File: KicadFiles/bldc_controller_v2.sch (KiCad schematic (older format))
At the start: 183 parts, among them J1 Conn_01x06_Male, J10 Conn_01x02_Female, J11 Conn_01x02_Female, J12 Conn_01x02_Female, J13 Conn_01x02_Female, J14 Conn_01x02_Female, J15 Conn_01x04_Male, J2 Conn_01x03_Male, J3 Conn_01x03_Male, J4 Screw_Terminal, J5 Conn_01x02_Female, J9 Conn_01x02_Female, Q1 DMN65D8L-7, Q10 IRLB8721PBF, Q11 IRLB8721PBF, Q2 DMN65D8L-7, Q3 DMN65D8L-7, Q5 IRF4905, Q6 IRLB8721PBF, Q7 IRLB8721PBF, Q8 IRLB8721PBF, Q9 IRLB8721PBF, SW1 D6C50 F1 LFS, SW2 D6C40 F1 LFS, SW3 1301.9314, SW4 1301.9314, SW5 SW_Push_DPDT, U1 ATmega328P-PU, U2 uA7810, U3 LM7805_TO220, U4 MCP601-xP, U5 LM339, U6 IRS2004, U7 IRS2004, U8 IRS2004, U9 NSL-32, Y1 9B-16.000MBBK-B

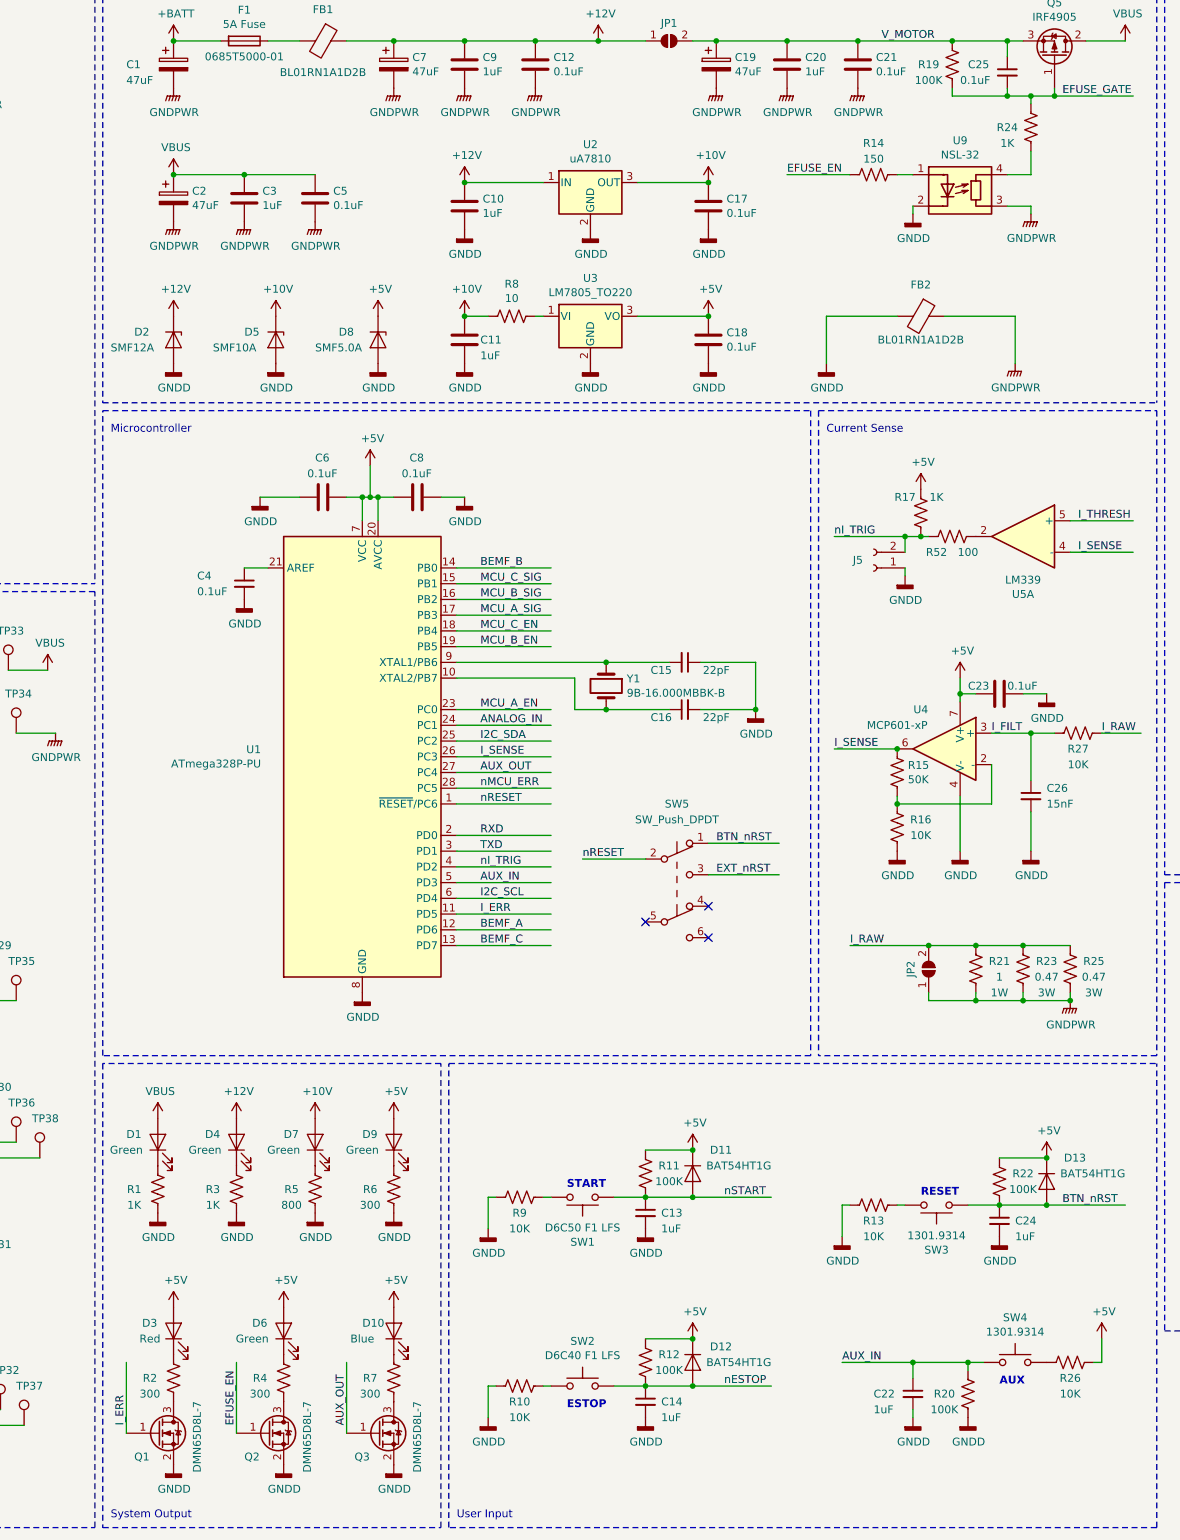
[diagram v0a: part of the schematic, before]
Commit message: Added Optoisolator
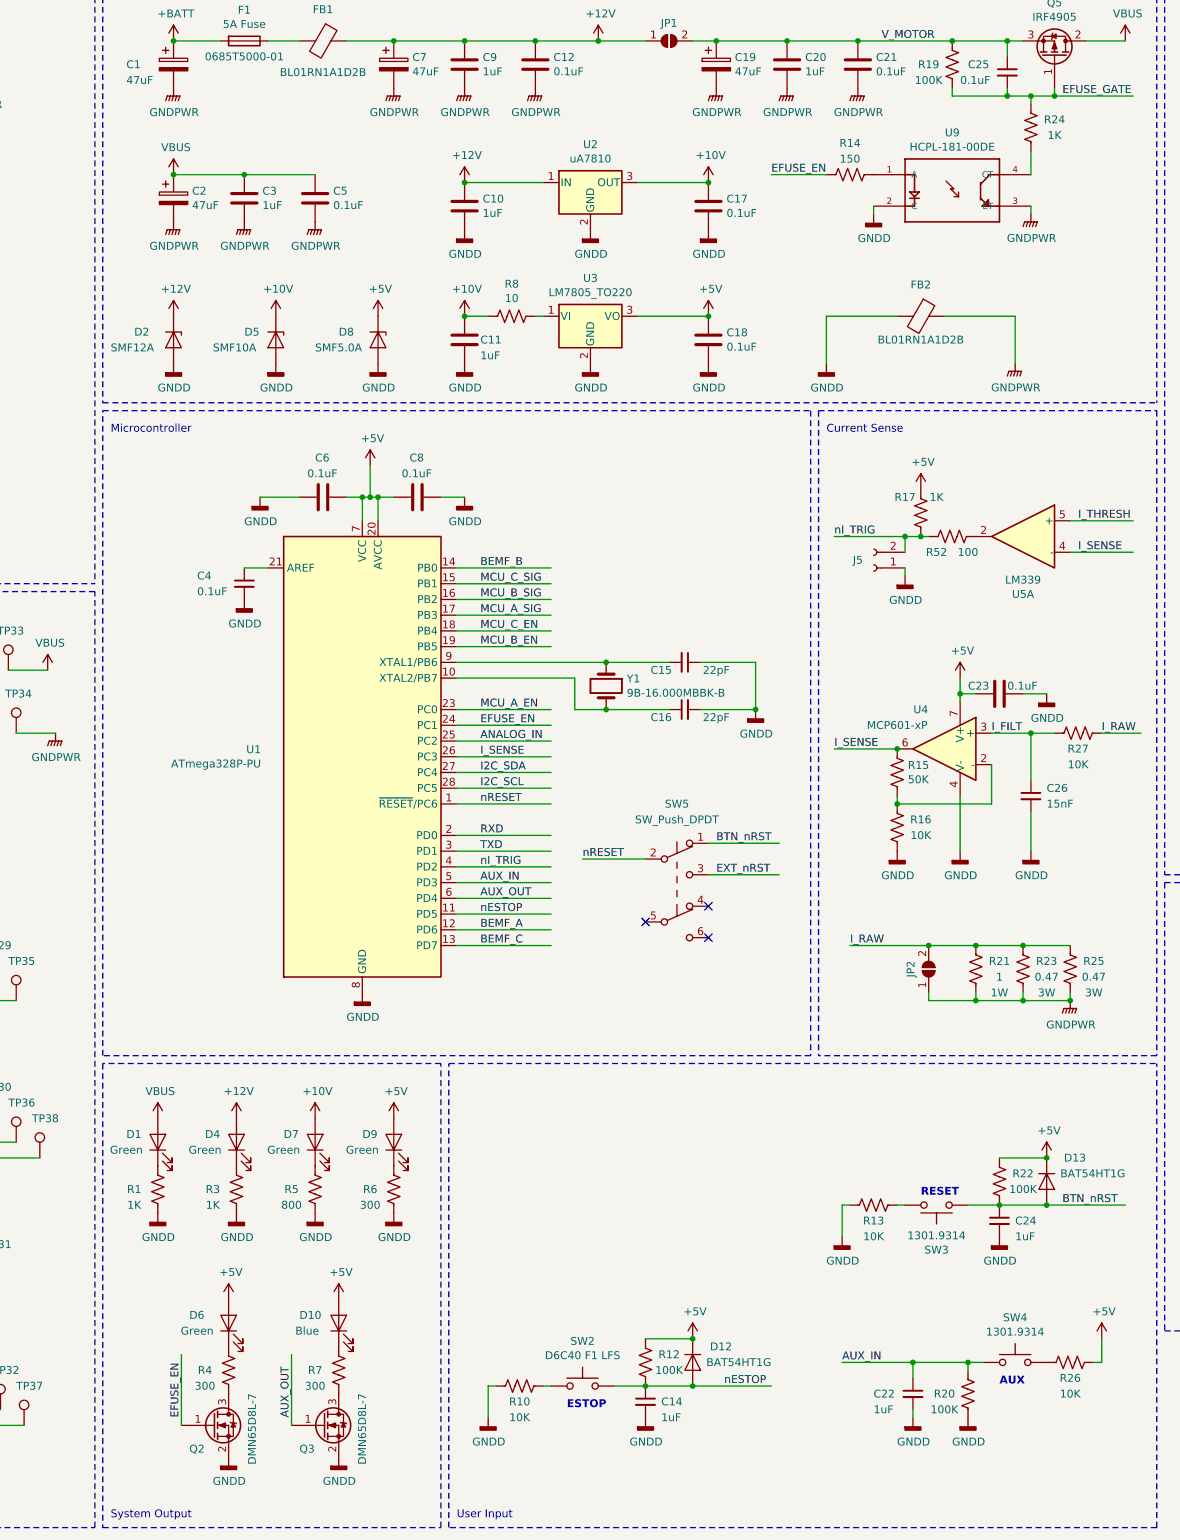
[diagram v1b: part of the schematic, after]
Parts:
- removed C13: 1uF, Capacitor_SMD:C_0805_2012Metric_Pad1.15x1.40mm_HandSolder, symbol Device:C_Small
- removed D11: BAT54HT1G, Diode_SMD:D_SOD-323_HandSoldering, symbol Diode:1N914
- removed D3: LTST-C171KRKT, LED_SMD:LED_0805_2012Metric_Pad1.15x1.40mm_HandSolder, symbol Device:LED
- removed Q1: DMN65D8L-7, Package_TO_SOT_SMD:SOT-23, symbol Transistor_FET:DMN67D7L
- removed R11: 100K, Resistor_SMD:R_0805_2012Metric_Pad1.15x1.40mm_HandSolder, symbol Device:R_US
- removed R2: 300, Resistor_SMD:R_0805_2012Metric_Pad1.15x1.40mm_HandSolder, symbol Device:R_US
- removed R9: 10K, Resistor_SMD:R_0805_2012Metric_Pad1.15x1.40mm_HandSolder, symbol Device:R_US
- removed SW1: D6C50 F1 LFS, Button_Switch_THT:Pushbutton_Switch_TH, symbol Switch:SW_Push
- removed U9: NSL-32, symbol Isolator:NSL-32
- added U9: HCPL-181-00DE, HCPL-181:SOIC254P700X220-4N, symbol HCPL-181-00DE:HCPL-181-00DE
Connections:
- net labels removed: I_ERR, nMCU_ERR, nSTART
- wire segments 340 -> 329
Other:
- note removed: "START"
- moved on the sheet: D10, D6, Q2, Q3, R14, R4, R7

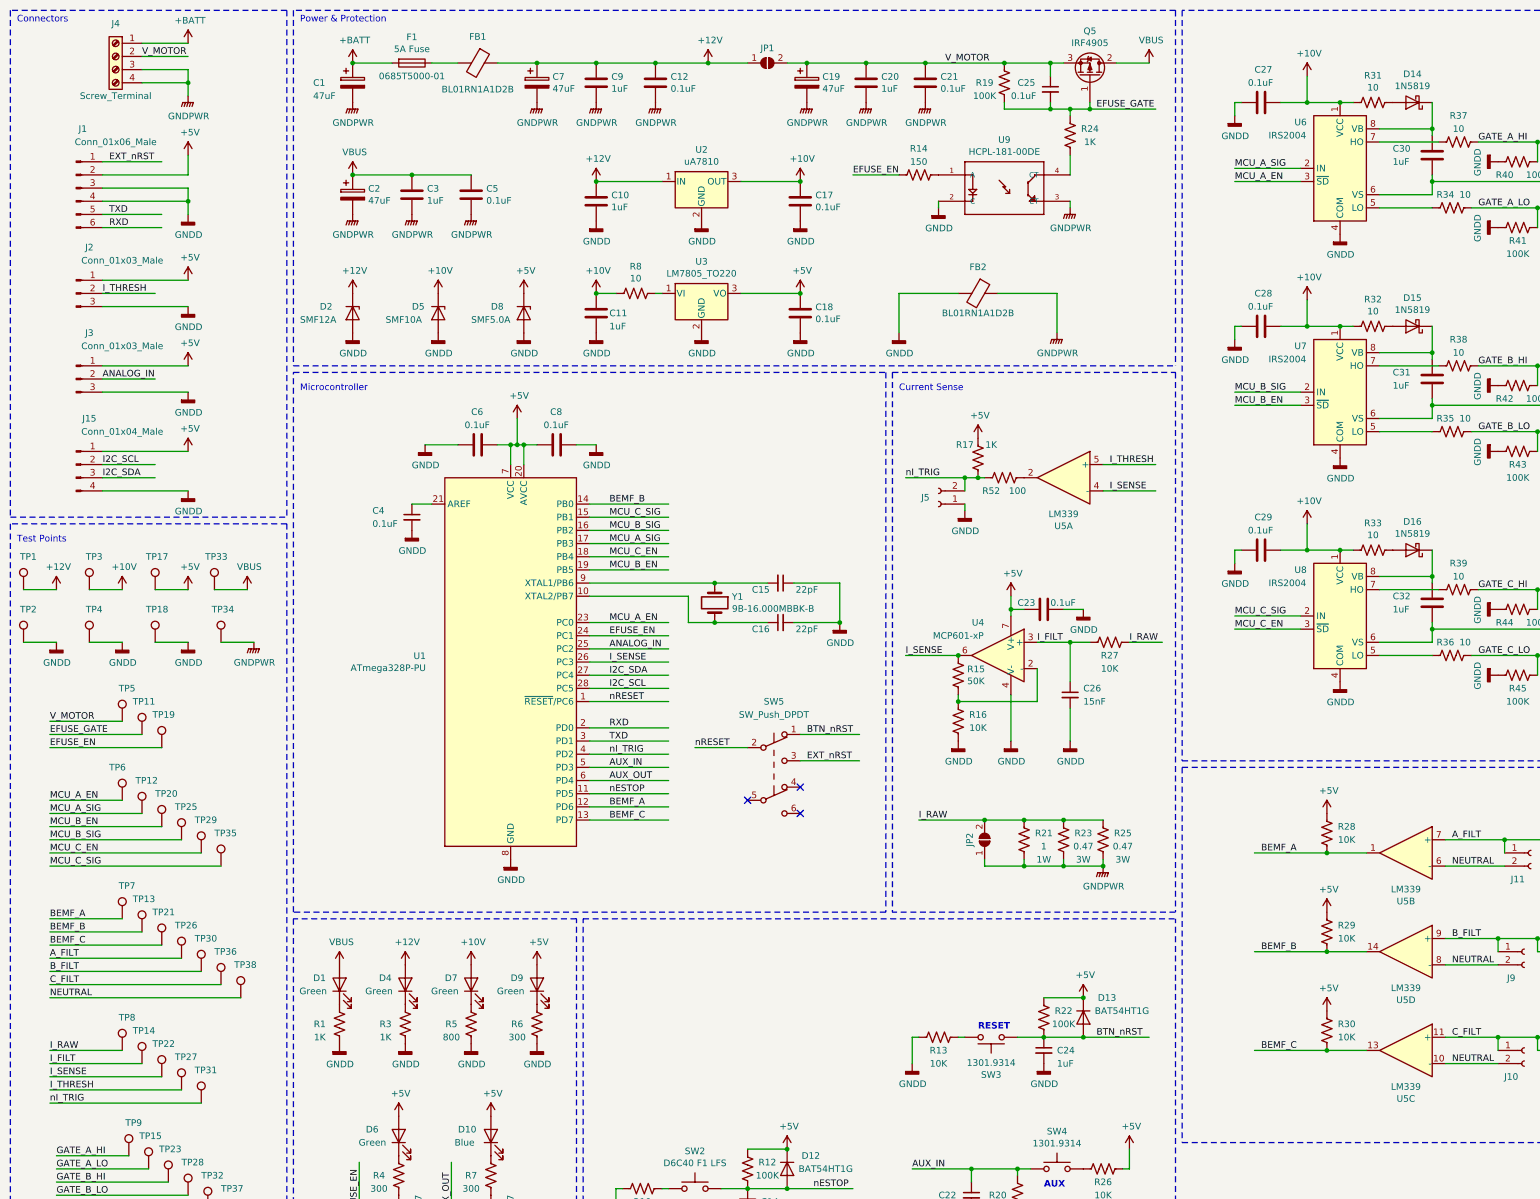
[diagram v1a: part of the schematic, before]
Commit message: Updated Major Parts Placement
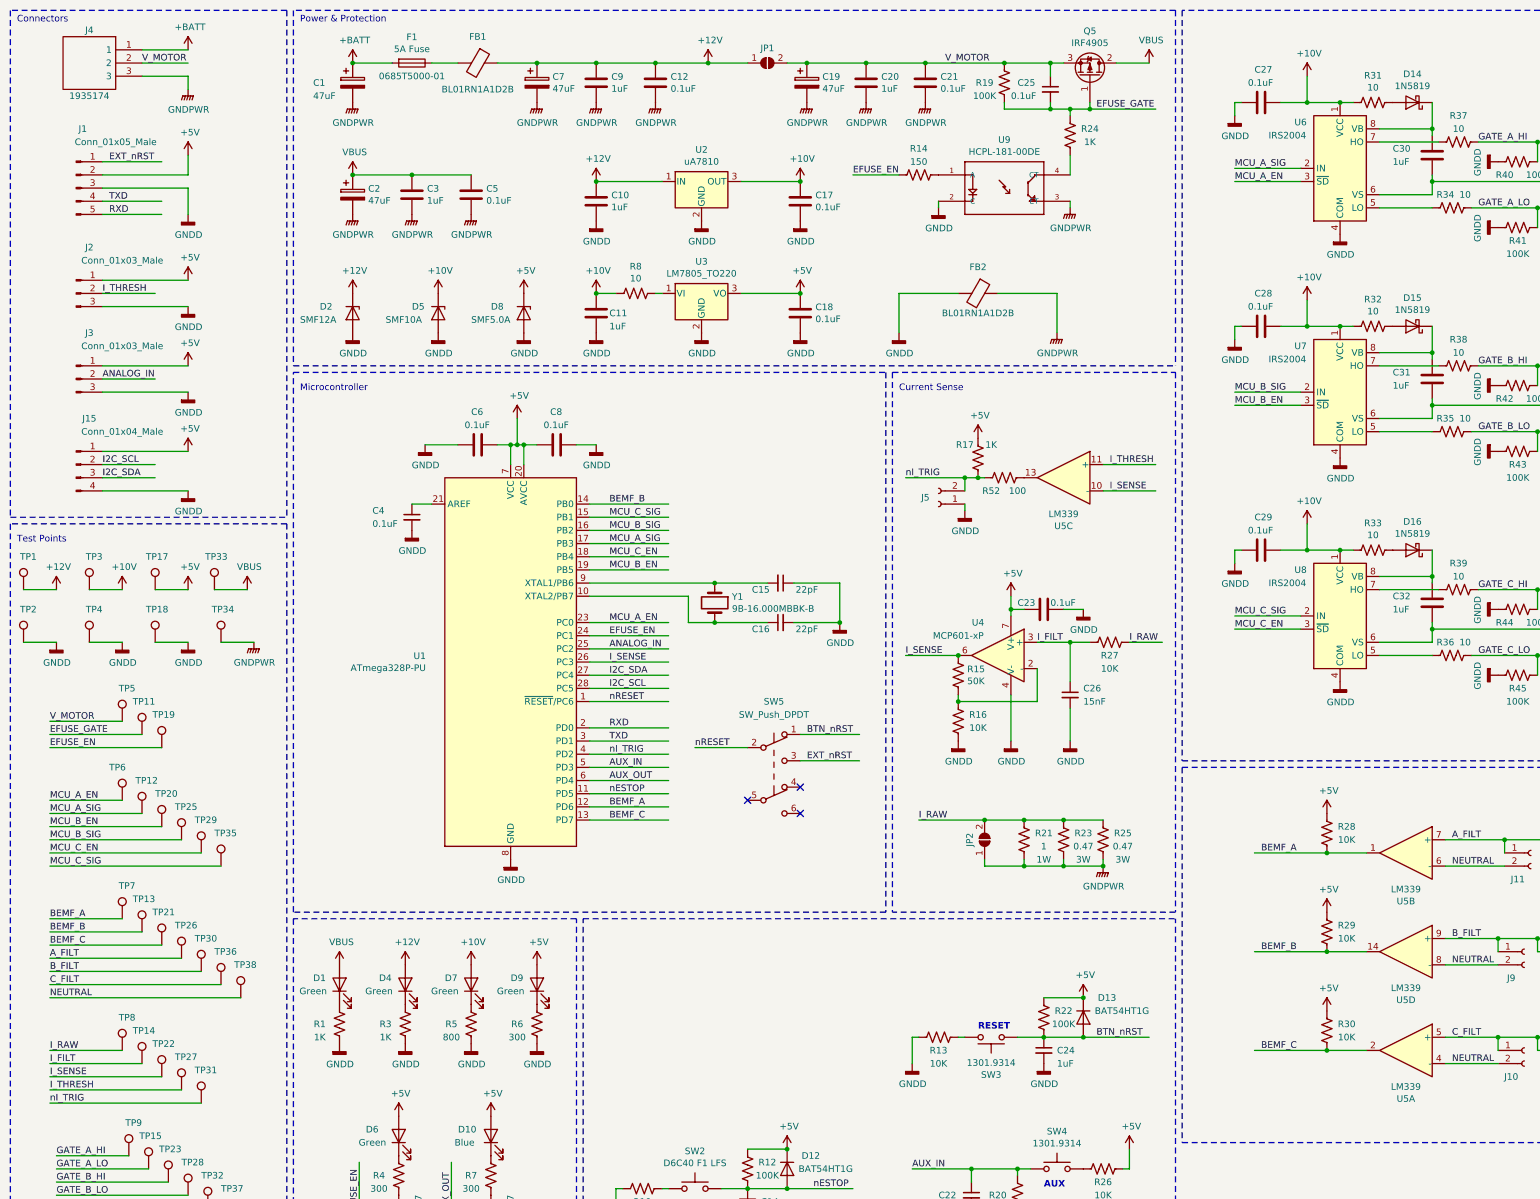
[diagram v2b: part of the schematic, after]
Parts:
- removed J1: Conn_01x06_Male, Connector_PinHeader_2.54mm:PinHeader_1x06_P2.54mm_Vertical, symbol Connector:Conn_01x06_Male
- removed J4: Screw_Terminal, Connector:Terminal_Block_4Pin_TH, symbol Connector:Screw_Terminal_01x04
- added J1: Conn_01x05_Male, Connector_PinHeader_2.54mm:PinHeader_1x05_P2.54mm_Vertical, symbol Connector:Conn_01x05_Male
- added J4: 1935174, 1935174:SHDR3W110P0X500_1X3_1500X900X1140P, symbol 1935174:1935174
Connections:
- wire segments 329 -> 325
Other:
- moved on the sheet: U5A, U5C
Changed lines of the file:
@@
 Text Label 1800 1750 0    50   ~ 0
 EXT_nRST
-Text Label 1800 2150 0    50   ~ 0
+Text Label 1800 2050 0    50   ~ 0
 TXD
-Text Label 1800 2250 0    50   ~ 0
+Text Label 1800 2150 0    50   ~ 0
 RXD
 $Comp
@@
 L power:+BATT #PWR05
 U 1 1 5DC4550F
-P 2400 850
-F 0 "#PWR05" H 2400 700 50  0001 C CNN
-F 1 "+BATT" H 2415 1023 50  0000 C CNN
-F 2 "" H 2400 850 50  0001 C CNN
-F 3 "" H 2400 850 50  0001 C CNN
-	1    2400 850
+P 2400 900
+F 0 "#PWR05" H 2400 750 50  0001 C CNN
+F 1 "+BATT" H 2415 1073 50  0000 C CNN
+F 2 "" H 2400 900 50  0001 C CNN
+F 3 "" H 2400 900 50  0001 C CNN
+	1    2400 900
 	1    0    0    -1
 $EndComp
@@
 	12650 2250 12650 2100
 $Comp
-L power:GNDPWR #PWR06
-U 1 1 5E79C61A
-P 2400 1250
-F 0 "#PWR06" H 2400 1050 50  0001 C CNN
-F 1 "GNDPWR" H 2404 1096 50  0000 C CNN
-F 2 "" H 2400 1200 50  0001 C CNN
-F 3 "" H 2400 1200 50  0001 C CNN
-	1    2400 1250
-	1    0    0    -1
-$EndComp
-$Comp
 L Jumper:SolderJumper_2_Open JP1
 U 1 1 5E8AD92E
@@
 	11900 1600 11450 1600
 Wire Wire Line
-	2050 850  2400 850
-Wire Wire Line
-	2050 1050 2400 1050
+	2050 900  2400 900
 Wire Wire Line
-	2400 1050 2400 1150
-Wire Wire Line
-	2050 1150 2400 1150
-Connection ~ 2400 1150
-Wire Wire Line
-	2400 1150 2400 1250
+	2050 1100 2400 1100
 $Comp
 L Device:C C20
@@
 Text Label 8150 1000 0    50   ~ 0
 V_MOTOR
-Text Label 2050 950  0    50   ~ 0
+Text Label 2050 1000 0    50   ~ 0
 V_MOTOR
 Wire Wire Line
-	2050 950  2400 950
+	2050 1000 2400 1000
 Wire Wire Line
 	5050 1000 5500 1000
@@
 L Comparator:LM339 U5
 U 3 1 5E59B0A8
-P 11650 8500
-F 0 "U5" H 11650 8133 50  0000 C CNN
-F 1 "LM339" H 11650 8224 50  0000 C CNN
-F 2 "Package_DIP:DIP-14_W7.62mm" H 11600 8600 50  0001 C CNN
-F 3 "http://www.ti.com/lit/ds/symlink/lm339.pdf" H 11700 8700 50  0001 C CNN
-	3    11650 8500
+P 9050 4150
+F 0 "U5" H 9050 3783 50  0000 C CNN
+F 1 "LM339" H 9050 3874 50  0000 C CNN
+F 2 "Package_DIP:DIP-14_W7.62mm" H 9000 4250 50  0001 C CNN
+F 3 "http://www.ti.com/lit/ds/symlink/lm339.pdf" H 9100 4350 50  0001 C CNN
+	3    9050 4150
 	-1   0    0    -1
 $EndComp
@@
 Connection ~ 12350 8400
 Wire Wire Line
-	1750 2250 2200 2250
-Wire Wire Line
 	1750 2150 2200 2150
 Wire Wire Line
+	1750 2050 2200 2050
+Wire Wire Line
 	1750 1850 2400 1850
 Wire Wire Line
 	1750 1950 2400 1950
 Wire Wire Line
-	2400 1950 2400 2050
-Wire Wire Line
-	1750 2050 2400 2050
-Connection ~ 2400 2050
-Wire Wire Line
-	2400 2050 2400 2150
-Wire Wire Line
 	1750 2750 2150 2750
 Text Label 1750 2750 0    50   ~ 0
@@
 Wire Notes Line
 	1050 4450 3150 4450
-$Comp
-L Connector:Screw_Terminal_01x04 J4
-U 1 1 5DDB786E
-P 1850 950
-F 0 "J4" H 1850 1200 50  0000 C CNN
-F 1 "Screw_Terminal" H 1850 650 50  0000 C CNN
-F 2 "Connector:Terminal_Block_4Pin_TH" H 1850 950 50  0001 C CNN
-F 3 "~" H 1850 950 50  0001 C CNN
-	1    1850 950
-	-1   0    0    -1
-$EndComp
-$Comp
-L Connector:Conn_01x06_Male J1
-U 1 1 5E521BF3
-P 1550 1950
-F 0 "J1" H 1600 2400 50  0000 C CNN
-F 1 "Conn_01x06_Male" H 1850 2300 50  0000 C CNN
-F 2 "Connector_PinHeader_2.54mm:PinHeader_1x06_P2.54mm_Vertical" H 1550 1950 50  0001 C CNN
-F 3 "~" H 1550 1950 50  0001 C CNN
-	1    1550 1950
-	1    0    0    -1
-$EndComp
 Wire Notes Line
 	3150 600  3150 4450
@@
 L Comparator:LM339 U5
 U 1 1 5DD3A6BE
-P 9050 4150
-F 0 "U5" H 9050 3783 50  0000 C CNN
-F 1 "LM339" H 9050 3874 50  0000 C CNN
-F 2 "Package_DIP:DIP-14_W7.62mm" H 9000 4250 50  0001 C CNN
-F 3 "http://www.ti.com/lit/ds/symlink/lm339.pdf" H 9100 4350 50  0001 C CNN
-	1    9050 4150
+P 11650 8500
+F 0 "U5" H 11650 8133 50  0000 C CNN
+F 1 "LM339" H 11650 8224 50  0000 C CNN
+F 2 "Package_DIP:DIP-14_W7.62mm" H 11600 8600 50  0001 C CNN
+F 3 "http://www.ti.com/lit/ds/symlink/lm339.pdf" H 11700 8700 50  0001 C CNN
+	1    11650 8500
 	-1   0    0    -1
 $EndComp
@@
 Text Label 5600 6350 0    50   ~ 0
 AUX_IN
+Wire Wire Line
+	2400 1100 2400 1200
+$Comp
+L power:GNDPWR #PWR06
+U 1 1 5E79C61A
+P 2400 1200
+F 0 "#PWR06" H 2400 1000 50  0001 C CNN
+F 1 "GNDPWR" H 2404 1046 50  0000 C CNN
+F 2 "" H 2400 1150 50  0001 C CNN
+F 3 "" H 2400 1150 50  0001 C CNN
+	1    2400 1200
+	1    0    0    -1
+$EndComp
+$Comp
+L 1935174:1935174 J4
+U 1 1 5E81481B
+P 2050 900
+F 0 "J4" H 2450 1050 50  0000 C CNN
+F 1 "1935174" H 2450 550 50  0000 C CNN
+F 2 "1935174:SHDR3W110P0X500_1X3_1500X900X1140P" H 2700 1000 50  0001 L CNN
+F 3 "https://componentsearchengine.com/Datasheets/1/1935174.pdf" H 2700 900 50  0001 L CNN
+F 4 "3 WAY SCREW TERMINAL BLOCK 5MM PITCH Phoenix Contact Non-Fused Terminal Block, 3 Way, Solder Terminals, 26 ??? 14 AWG Through Hole, Nylon, 250 V" H 2700 800 50  0001 L CNN "Description"
+F 5 "11.4" H 2700 700 50  0001 L CNN "Height"
+F 6 "651-1935174" H 2700 600 50  0001 L CNN "Mouser Part Number"
+F 7 "https://www.mouser.com/Search/Refine.aspx?Keyword=651-1935174" H 2700 500 50  0001 L CNN "Mouser Price/Stock"
+F 8 "Phoenix Contact" H 2700 400 50  0001 L CNN "Manufacturer_Name"
+F 9 "1935174" H 2700 300 50  0001 L CNN "Manufacturer_Part_Number"
+	1    2050 900
+	-1   0    0    -1
+$EndComp
+$Comp
+L Connector:Conn_01x05_Male J1
+U 1 1 5E9F193C
+P 1550 1950
+F 0 "J1" H 1600 2400 50  0000 C CNN
+F 1 "Conn_01x05_Male" H 1850 2300 50  0000 C CNN
+F 2 "Connector_PinHeader_2.54mm:PinHeader_1x05_P2.54mm_Vertical" H 1550 1950 50  0001 C CNN
+F 3 "~" H 1550 1950 50  0001 C CNN
+	1    1550 1950
+	1    0    0    -1
+$EndComp
+Wire Wire Line
+	2400 1950 2400 2150
 $EndSCHEMATC
